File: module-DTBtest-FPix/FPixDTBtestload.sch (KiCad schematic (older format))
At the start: 13 parts, among them J1 CONN-SMK20, P15 RTD+, P16 RTD-

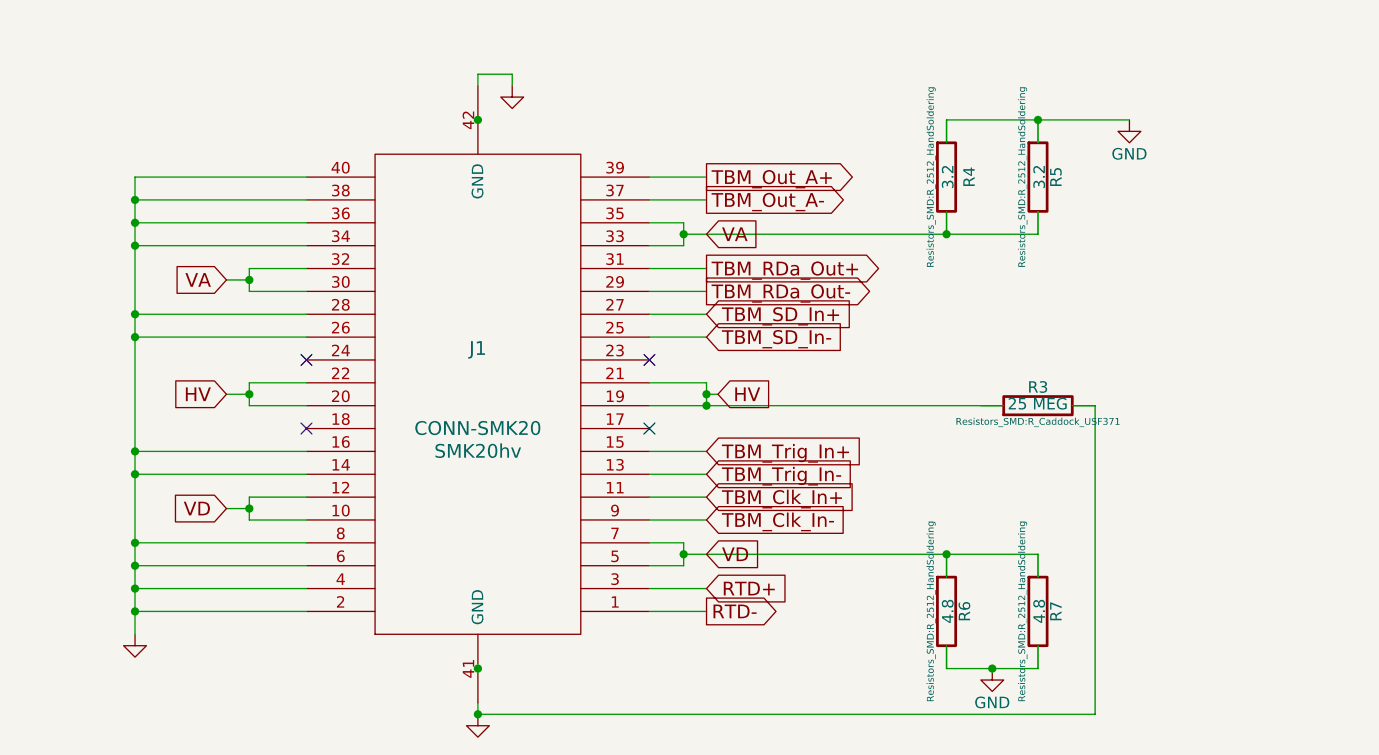
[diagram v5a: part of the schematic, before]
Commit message: Adjusted pin-out of connector to match other end of cable.
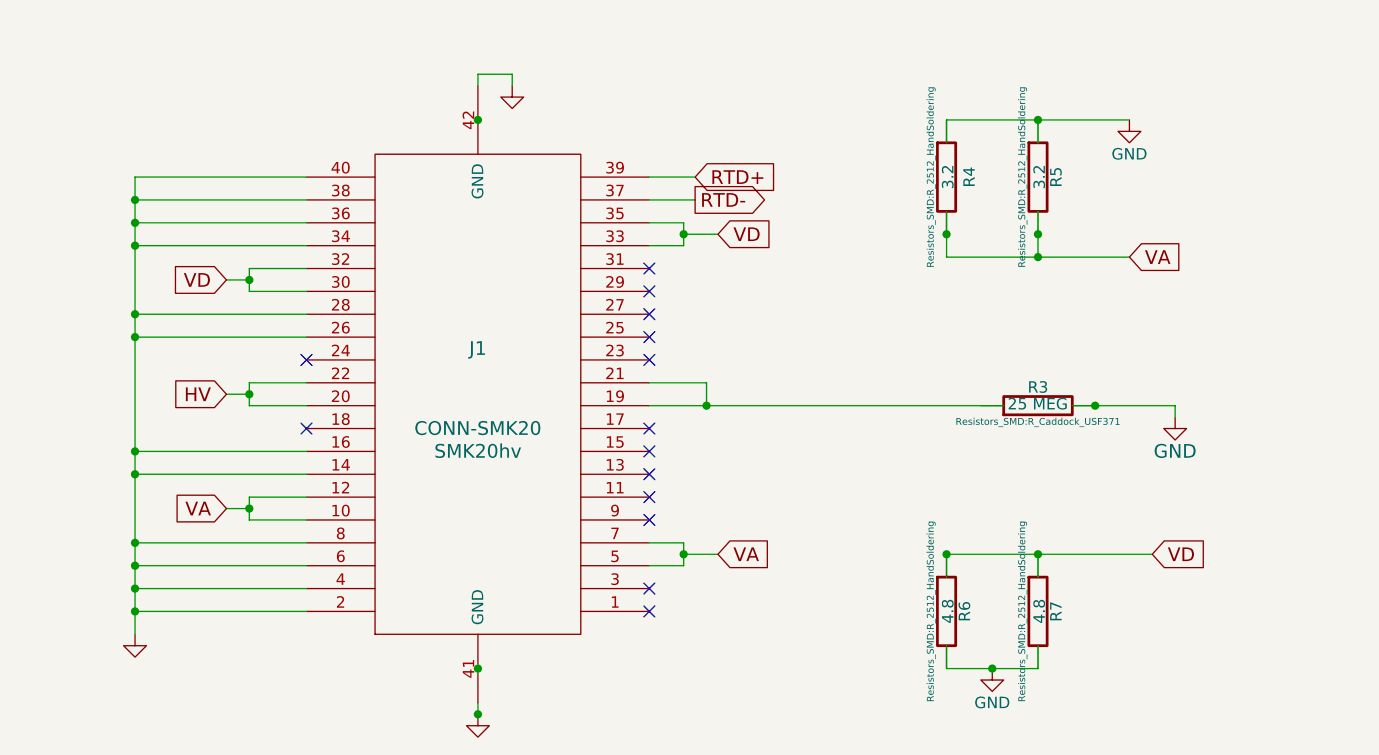
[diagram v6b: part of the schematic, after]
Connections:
- net labels removed: TBM_Clk_In+, TBM_Clk_In-, TBM_Out_A+, TBM_Out_A-, TBM_RDa_Out+, TBM_RDa_Out-, TBM_SD_In+, TBM_SD_In-, TBM_Trig_In+, TBM_Trig_In-
- wire segments 79 -> 69
- no-connect marks 4 -> 14
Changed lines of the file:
@@
 LIBS:memory
 LIBS:xilinx
+LIBS:special
 LIBS:microcontrollers
 LIBS:dsp
@@
 	1    0    0    -1
 $EndComp
-Text GLabel 6650 3650 2    60   Output ~ 0
-TBM_Out_A+
-Text GLabel 6650 3900 2    60   Input ~ 0
+Text GLabel 6700 5300 2    60   Input ~ 0
 VA
-Text GLabel 4550 5100 0    60   Input ~ 0
+Text GLabel 4550 4100 0    60   Input ~ 0
 VD
 $Comp
@@
 	1    0    0    -1
 $EndComp
-Text GLabel 6700 4600 2    60   Input ~ 0
-HV
 Text GLabel 4550 4600 0    60   Input ~ 0
 HV
-Text GLabel 6650 5450 2    60   Input ~ 0
+Text GLabel 6600 3650 2    60   Input ~ 0
 RTD+
-Text GLabel 6650 5550 2    60   Output ~ 0
+Text GLabel 6600 3750 2    60   Output ~ 0
 RTD-
-Text GLabel 6650 3750 2    60   Output ~ 0
-TBM_Out_A-
-Text GLabel 6650 4050 2    60   Output ~ 0
-TBM_RDa_Out+
-Text GLabel 6650 4150 2    60   Output ~ 0
-TBM_RDa_Out-
-Text GLabel 6650 4250 2    60   Input ~ 0
-TBM_SD_In+
-Text GLabel 6650 4350 2    60   Input ~ 0
-TBM_SD_In-
-Text GLabel 6650 4850 2    60   Input ~ 0
-TBM_Trig_In+
-Text GLabel 6650 4950 2    60   Input ~ 0
-TBM_Trig_In-
-Text GLabel 6650 5050 2    60   Input ~ 0
-TBM_Clk_In+
-Text GLabel 6650 5150 2    60   Input ~ 0
-TBM_Clk_In-
 NoConn ~ 4900 4450
 NoConn ~ 4900 4750
@@
 	1    0    0    -1
 $EndComp
-Text GLabel 4550 4100 0    60   Input ~ 0
+Text GLabel 4550 5100 0    60   Input ~ 0
 VA
 $Comp
@@
 	1    0    0    -1
 $EndComp
-Text GLabel 6650 5300 2    60   Input ~ 0
+Text GLabel 6700 3900 2    60   Input ~ 0
 VD
 Text Notes 6600 950  0    60   ~ 0
@@
 Connection ~ 7400 2300
 Wire Wire Line
-	6650 4600 6700 4600
-Connection ~ 6650 4600
-Wire Wire Line
 	4900 4550 4650 4550
 Wire Wire Line
@@
 Connection ~ 4150 5550
 Wire Wire Line
-	4550 4100 4650 4100
-Wire Wire Line
 	4650 4050 4650 4150
 Wire Wire Line
@@
 Connection ~ 4650 4100
 Wire Wire Line
-	4550 5100 4650 5100
-Wire Wire Line
 	4650 5050 4650 5150
 Wire Wire Line
@@
 Connection ~ 4650 5100
 Wire Wire Line
-	6400 3650 6650 3650
-Wire Wire Line
-	6400 3750 6650 3750
-Wire Wire Line
 	6400 3850 6550 3850
 Wire Wire Line
 	6550 3850 6550 3950
-Wire Wire Line
-	6550 3900 8100 3900
 Wire Wire Line
 	6550 3950 6400 3950
 Connection ~ 6550 3900
 Wire Wire Line
-	6400 4050 6650 4050
-Wire Wire Line
-	6400 4150 6650 4150
-Wire Wire Line
-	6400 4250 6650 4250
-Wire Wire Line
-	6400 4350 6650 4350
-Wire Wire Line
 	6400 4550 6650 4550
 Wire Wire Line
 	6400 4650 7950 4650
 Wire Wire Line
-	6400 4850 6650 4850
-Wire Wire Line
-	6400 4950 6650 4950
-Wire Wire Line
-	6400 5050 6650 5050
-Wire Wire Line
-	6400 5150 6650 5150
-Wire Wire Line
 	6400 5250 6550 5250
 Wire Wire Line
 	6550 5250 6550 5350
-Wire Wire Line
-	6550 5300 8100 5300
 Wire Wire Line
 	6550 5350 6400 5350
 Connection ~ 6550 5300
-Wire Wire Line
-	6400 5450 6650 5450
-Wire Wire Line
-	6400 5550 6650 5550
 Wire Wire Line
 	7150 1100 7950 1100
@@
 	-1   0    0    1
 $EndComp
-Wire Wire Line
-	8350 4650 8350 6000
-Wire Wire Line
-	8350 6000 5650 6000
 Connection ~ 5650 6000
 Wire Wire Line
@@
 	8100 3400 8100 3500
 Wire Wire Line
-	7700 3900 7700 3800
-Wire Wire Line
-	8100 3900 8100 3800
+	7700 3800 7700 4000
+Wire Wire Line
+	8100 3800 8100 4000
 Wire Wire Line
 	7700 5400 7700 5300
@@
 	8100 5800 8100 5700
 Wire Wire Line
-	8250 4650 8350 4650
+	8250 4650 8700 4650
 $Comp
 L GND #PWR05
@@
 	6650 4550 6650 4650
 Connection ~ 6650 4650
+NoConn ~ 6400 4050
+NoConn ~ 6400 4150
+NoConn ~ 6400 4250
+NoConn ~ 6400 4350
+NoConn ~ 6400 4850
+NoConn ~ 6400 4950
+NoConn ~ 6400 5050
+NoConn ~ 6400 5150
+NoConn ~ 6400 5450
+NoConn ~ 6400 5550
+Wire Wire Line
+	6400 3650 6600 3650
+Wire Wire Line
+	6400 3750 6600 3750
+Wire Wire Line
+	4650 4100 4550 4100
+Wire Wire Line
+	4550 5100 4650 5100
+Text GLabel 8500 4000 2    60   Input ~ 0
+VA
+Wire Wire Line
+	7700 4000 8500 4000
+Connection ~ 8100 3900
+Connection ~ 8100 4000
+Text GLabel 8600 5300 2    60   Input ~ 0
+VD
+$Comp
+L GND #PWR?
+U 1 1 559D8FFC
+P 8700 4700
+F 0 "#PWR?" H 8700 4450 60  0001 C CNN
+F 1 "GND" H 8700 4550 60  0000 C CNN
+F 2 "" H 8700 4700 60  0000 C CNN
+F 3 "" H 8700 4700 60  0000 C CNN
+	1    8700 4700
+	1    0    0    -1
+$EndComp
+Wire Wire Line
+	8700 4650 8700 4700
+Connection ~ 8350 4650
+Connection ~ 8100 5300
+Wire Wire Line
+	6550 5300 6700 5300
+Wire Wire Line
+	6550 3900 6700 3900
+Wire Wire Line
+	7700 5300 8600 5300
 $EndSCHEMATC

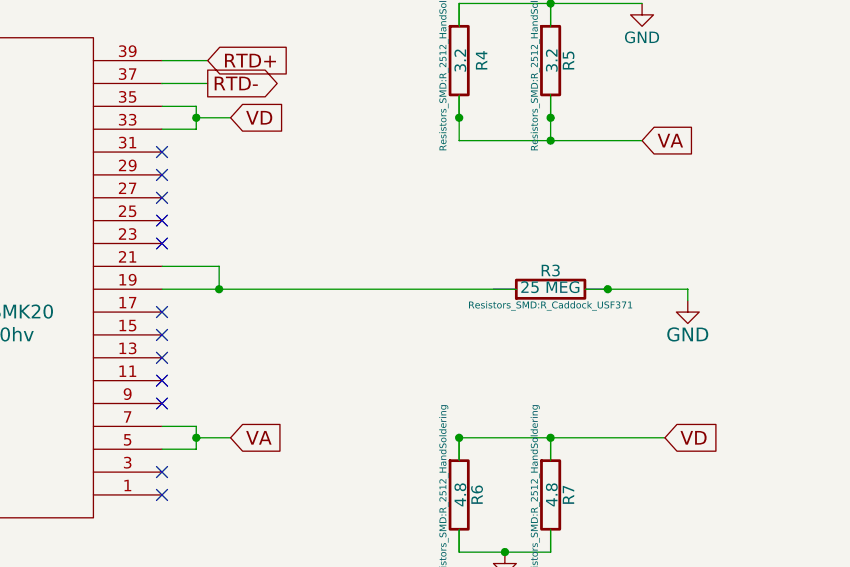
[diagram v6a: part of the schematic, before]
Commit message: first draft of connector on the right unfinished
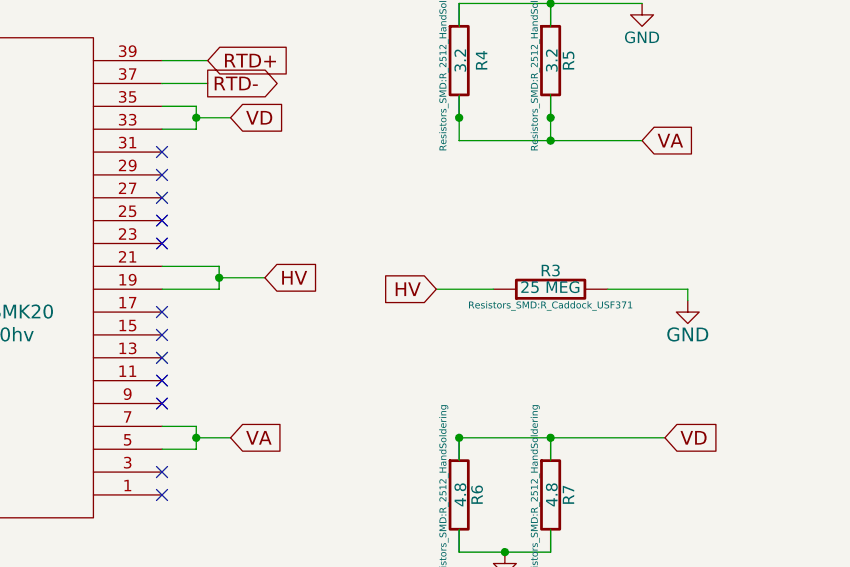
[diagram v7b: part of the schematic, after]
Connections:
- wire segments 69 -> 71
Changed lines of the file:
@@
 	1    0    0    -1
 $EndComp
-Connection ~ 7750 2300
-Connection ~ 7400 1100
-Connection ~ 7400 2300
-Wire Wire Line
-	4900 4550 4650 4550
-Wire Wire Line
-	4650 4550 4650 4650
-Wire Wire Line
-	4650 4600 4550 4600
-Wire Wire Line
-	4650 4650 4900 4650
-Connection ~ 4650 4600
-Wire Wire Line
-	5650 5950 5650 6000
-Wire Wire Line
-	5650 3250 5650 3200
-Wire Wire Line
-	5650 3200 5800 3200
-Wire Wire Line
-	5800 3200 5800 3250
-Wire Wire Line
-	4900 3650 4150 3650
-Wire Wire Line
-	4150 3650 4150 5650
-Wire Wire Line
-	4900 3750 4150 3750
-Connection ~ 4150 3750
-Wire Wire Line
-	4900 3850 4150 3850
-Connection ~ 4150 3850
-Wire Wire Line
-	4900 3950 4150 3950
-Connection ~ 4150 3950
-Wire Wire Line
-	4900 4250 4150 4250
-Connection ~ 4150 4250
-Wire Wire Line
-	4900 4350 4150 4350
-Connection ~ 4150 4350
-Wire Wire Line
-	4900 4850 4150 4850
-Connection ~ 4150 4850
-Wire Wire Line
-	4900 4950 4150 4950
-Connection ~ 4150 4950
-Wire Wire Line
-	4900 5250 4150 5250
-Connection ~ 4150 5250
-Wire Wire Line
-	4900 5350 4150 5350
-Connection ~ 4150 5350
-Wire Wire Line
-	4900 5450 4150 5450
-Connection ~ 4150 5450
-Wire Wire Line
-	4900 5550 4150 5550
-Connection ~ 4150 5550
-Wire Wire Line
-	4650 4050 4650 4150
-Wire Wire Line
-	4650 4050 4900 4050
-Wire Wire Line
-	4650 4150 4900 4150
-Connection ~ 4650 4100
-Wire Wire Line
-	4650 5050 4650 5150
-Wire Wire Line
-	4650 5050 4900 5050
-Wire Wire Line
-	4650 5150 4900 5150
-Connection ~ 4650 5100
-Wire Wire Line
-	6400 3850 6550 3850
-Wire Wire Line
-	6550 3850 6550 3950
-Wire Wire Line
-	6550 3950 6400 3950
-Connection ~ 6550 3900
-Wire Wire Line
-	6400 4550 6650 4550
-Wire Wire Line
-	6400 4650 7950 4650
-Wire Wire Line
-	6400 5250 6550 5250
-Wire Wire Line
-	6550 5250 6550 5350
-Wire Wire Line
-	6550 5350 6400 5350
-Connection ~ 6550 5300
-Wire Wire Line
-	7150 1100 7950 1100
-Connection ~ 7750 1700
 $Comp
 L R R4
@@
 	1    0    0    -1
 $EndComp
-Connection ~ 5650 5800
-Connection ~ 5650 3400
 $Comp
 L R R5
@@
 	1    0    0    -1
 $EndComp
-Connection ~ 7700 3900
 $Comp
 L R R7
@@
 	1    0    0    -1
 $EndComp
-Connection ~ 7700 5300
 $Comp
 L CONN-SMK20 J1
@@
 	-1   0    0    1
 $EndComp
-Connection ~ 5650 6000
-Wire Wire Line
-	7750 1100 7750 1200
-Wire Wire Line
-	7750 1500 7750 1850
-Wire Wire Line
-	7750 2300 7750 2150
-Wire Wire Line
-	7700 3500 7700 3400
-Wire Wire Line
-	8100 3400 8100 3500
-Wire Wire Line
-	7700 3800 7700 4000
-Wire Wire Line
-	8100 3800 8100 4000
-Wire Wire Line
-	7700 5400 7700 5300
-Wire Wire Line
-	8100 5300 8100 5400
-Wire Wire Line
-	7700 5800 7700 5700
-Wire Wire Line
-	8100 5800 8100 5700
-Wire Wire Line
-	8250 4650 8700 4650
 $Comp
 L GND #PWR05
@@
 	1    0    0    -1
 $EndComp
-Wire Wire Line
-	7700 3400 8500 3400
-Connection ~ 8100 3400
 $Comp
 L GND #PWR06
@@
 	1    0    0    -1
 $EndComp
-Wire Wire Line
-	7700 5800 8100 5800
-Connection ~ 7900 5800
 $Comp
 L GND #PWR07
@@
 	1    0    0    -1
 $EndComp
-Wire Wire Line
-	2800 2150 2800 1900
-Wire Wire Line
-	2800 1900 3200 1900
-Wire Wire Line
-	3800 1900 4050 1900
-Wire Wire Line
-	4050 1900 4050 2150
 $Comp
 L JUMPER3 JP2
@@
 	0    1    1    0
 $EndComp
-Wire Wire Line
-	7750 1700 8300 1700
-Wire Wire Line
-	7150 2300 8400 2300
-Wire Wire Line
-	8400 2300 8400 1950
 $Comp
 L R R8
@@
 	0    1    1    0
 $EndComp
-Connection ~ 7750 1100
-Wire Wire Line
-	8250 1100 8400 1100
-Wire Wire Line
-	8400 1100 8400 1450
-Wire Wire Line
-	6650 4550 6650 4650
-Connection ~ 6650 4650
 NoConn ~ 6400 4050
 NoConn ~ 6400 4150
@@
 NoConn ~ 6400 5450
 NoConn ~ 6400 5550
-Wire Wire Line
-	6400 3650 6600 3650
-Wire Wire Line
-	6400 3750 6600 3750
-Wire Wire Line
-	4650 4100 4550 4100
-Wire Wire Line
-	4550 5100 4650 5100
 Text GLabel 8500 4000 2    60   Input ~ 0
 VA
-Wire Wire Line
-	7700 4000 8500 4000
-Connection ~ 8100 3900
-Connection ~ 8100 4000
 Text GLabel 8600 5300 2    60   Input ~ 0
 VD
@@
 	1    0    0    -1
 $EndComp
+Text GLabel 6850 4600 2    60   Input ~ 0
+HV
+Text GLabel 7600 4650 0    60   Input ~ 0
+HV
+Connection ~ 7750 2300
+Connection ~ 7400 1100
+Connection ~ 7400 2300
+Wire Wire Line
+	4900 4550 4650 4550
+Wire Wire Line
+	4650 4550 4650 4650
+Wire Wire Line
+	4650 4600 4550 4600
+Wire Wire Line
+	4650 4650 4900 4650
+Connection ~ 4650 4600
+Wire Wire Line
+	5650 5950 5650 6000
+Wire Wire Line
+	5650 3250 5650 3200
+Wire Wire Line
+	5650 3200 5800 3200
+Wire Wire Line
+	5800 3200 5800 3250
+Wire Wire Line
+	4900 3650 4150 3650
+Wire Wire Line
+	4150 3650 4150 5650
+Wire Wire Line
+	4900 3750 4150 3750
+Connection ~ 4150 3750
+Wire Wire Line
+	4900 3850 4150 3850
+Connection ~ 4150 3850
+Wire Wire Line
+	4900 3950 4150 3950
+Connection ~ 4150 3950
+Wire Wire Line
+	4900 4250 4150 4250
+Connection ~ 4150 4250
+Wire Wire Line
+	4900 4350 4150 4350
+Connection ~ 4150 4350
+Wire Wire Line
+	4900 4850 4150 4850
+Connection ~ 4150 4850
+Wire Wire Line
+	4900 4950 4150 4950
+Connection ~ 4150 4950
+Wire Wire Line
+	4900 5250 4150 5250
+Connection ~ 4150 5250
+Wire Wire Line
+	4900 5350 4150 5350
+Connection ~ 4150 5350
+Wire Wire Line
+	4900 5450 4150 5450
+Connection ~ 4150 5450
+Wire Wire Line
+	4900 5550 4150 5550
+Connection ~ 4150 5550
+Wire Wire Line
+	4650 4050 4650 4150
+Wire Wire Line
+	4650 4050 4900 4050
+Wire Wire Line
+	4650 4150 4900 4150
+Connection ~ 4650 4100
+Wire Wire Line
+	4650 5050 4650 5150
+Wire Wire Line
+	4650 5050 4900 5050
+Wire Wire Line
+	4650 5150 4900 5150
+Connection ~ 4650 5100
+Wire Wire Line
+	6400 3850 6550 3850
+Wire Wire Line
+	6550 3850 6550 3950
+Wire Wire Line
+	6550 3950 6400 3950
+Connection ~ 6550 3900
+Wire Wire Line
+	6400 4550 6650 4550
+Wire Wire Line
+	6400 5250 6550 5250
+Wire Wire Line
+	6550 5250 6550 5350
+Wire Wire Line
+	6550 5350 6400 5350
+Connection ~ 6550 5300
+Wire Wire Line
+	7150 1100 7950 1100
+Connection ~ 7750 1700
+Connection ~ 5650 5800
+Connection ~ 5650 3400
+Connection ~ 7700 3900
+Connection ~ 7700 5300
+Connection ~ 5650 6000
+Wire Wire Line
+	7750 1100 7750 1200
+Wire Wire Line
+	7750 1500 7750 1850
+Wire Wire Line
+	7750 2300 7750 2150
+Wire Wire Line
+	7700 3500 7700 3400
+Wire Wire Line
+	8100 3400 8100 3500
+Wire Wire Line
+	7700 3800 7700 4000
+Wire Wire Line
+	8100 3800 8100 4000
+Wire Wire Line
+	7700 5400 7700 5300
+Wire Wire Line
+	8100 5300 8100 5400
+Wire Wire Line
+	7700 5800 7700 5700
+Wire Wire Line
+	8100 5800 8100 5700
+Wire Wire Line
+	7700 3400 8500 3400
+Connection ~ 8100 3400
+Wire Wire Line
+	7700 5800 8100 5800
+Connection ~ 7900 5800
+Wire Wire Line
+	2800 2150 2800 1900
+Wire Wire Line
+	2800 1900 3200 1900
+Wire Wire Line
+	3800 1900 4050 1900
+Wire Wire Line
+	4050 1900 4050 2150
+Wire Wire Line
+	7750 1700 8300 1700
+Wire Wire Line
+	7150 2300 8400 2300
+Wire Wire Line
+	8400 2300 8400 1950
+Connection ~ 7750 1100
+Wire Wire Line
+	8250 1100 8400 1100
+Wire Wire Line
+	8400 1100 8400 1450
+Wire Wire Line
+	6400 3650 6600 3650
+Wire Wire Line
+	6400 3750 6600 3750
+Wire Wire Line
+	4650 4100 4550 4100
+Wire Wire Line
+	4550 5100 4650 5100
+Wire Wire Line
+	7700 4000 8500 4000
+Connection ~ 8100 3900
+Connection ~ 8100 4000
 Wire Wire Line
 	8700 4650 8700 4700
-Connection ~ 8350 4650
 Connection ~ 8100 5300
 Wire Wire Line
@@
 Wire Wire Line
 	7700 5300 8600 5300
+Wire Wire Line
+	6850 4600 6650 4600
+Wire Wire Line
+	6650 4550 6650 4650
+Wire Wire Line
+	6650 4650 6400 4650
+Connection ~ 6650 4600
+Wire Wire Line
+	8700 4650 8350 4650
+Wire Wire Line
+	7850 4650 7600 4650
 $EndSCHEMATC

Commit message: first draft of potentially finished load board? please check
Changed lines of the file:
@@
 VD
 $Comp
-L GND #PWR?
+L GND #PWR09
 U 1 1 559D8FFC
 P 8700 4700
-F 0 "#PWR?" H 8700 4450 60  0001 C CNN
+F 0 "#PWR09" H 8700 4450 60  0001 C CNN
 F 1 "GND" H 8700 4550 60  0000 C CNN
 F 2 "" H 8700 4700 60  0000 C CNN
@@
 Text GLabel 7600 4650 0    60   Input ~ 0
 HV
-Connection ~ 7750 2300
 Connection ~ 7400 1100
 Connection ~ 7400 2300
@@
 	6550 5350 6400 5350
 Connection ~ 6550 5300
-Wire Wire Line
-	7150 1100 7950 1100
 Connection ~ 7750 1700
 Connection ~ 5650 5800
@@
 Wire Wire Line
 	7750 1100 7750 1200
-Wire Wire Line
-	7750 1500 7750 1850
-Wire Wire Line
-	7750 2300 7750 2150
 Wire Wire Line
 	7700 3500 7700 3400
@@
 Wire Wire Line
 	7750 1700 8300 1700
-Wire Wire Line
-	7150 2300 8400 2300
-Wire Wire Line
-	8400 2300 8400 1950
 Connection ~ 7750 1100
-Wire Wire Line
-	8250 1100 8400 1100
 Wire Wire Line
 	8400 1100 8400 1450
@@
 Wire Wire Line
 	7850 4650 7600 4650
+Wire Wire Line
+	7150 2300 8400 2300
+Wire Wire Line
+	7750 2300 7750 2250
+Wire Wire Line
+	8400 2300 8400 1950
+Connection ~ 7750 2300
+Wire Wire Line
+	7750 1600 7750 1750
+Wire Wire Line
+	7150 1100 7850 1100
+Wire Wire Line
+	8350 1100 8400 1100
 $EndSCHEMATC
